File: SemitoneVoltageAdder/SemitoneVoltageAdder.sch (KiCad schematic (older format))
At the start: 9 parts

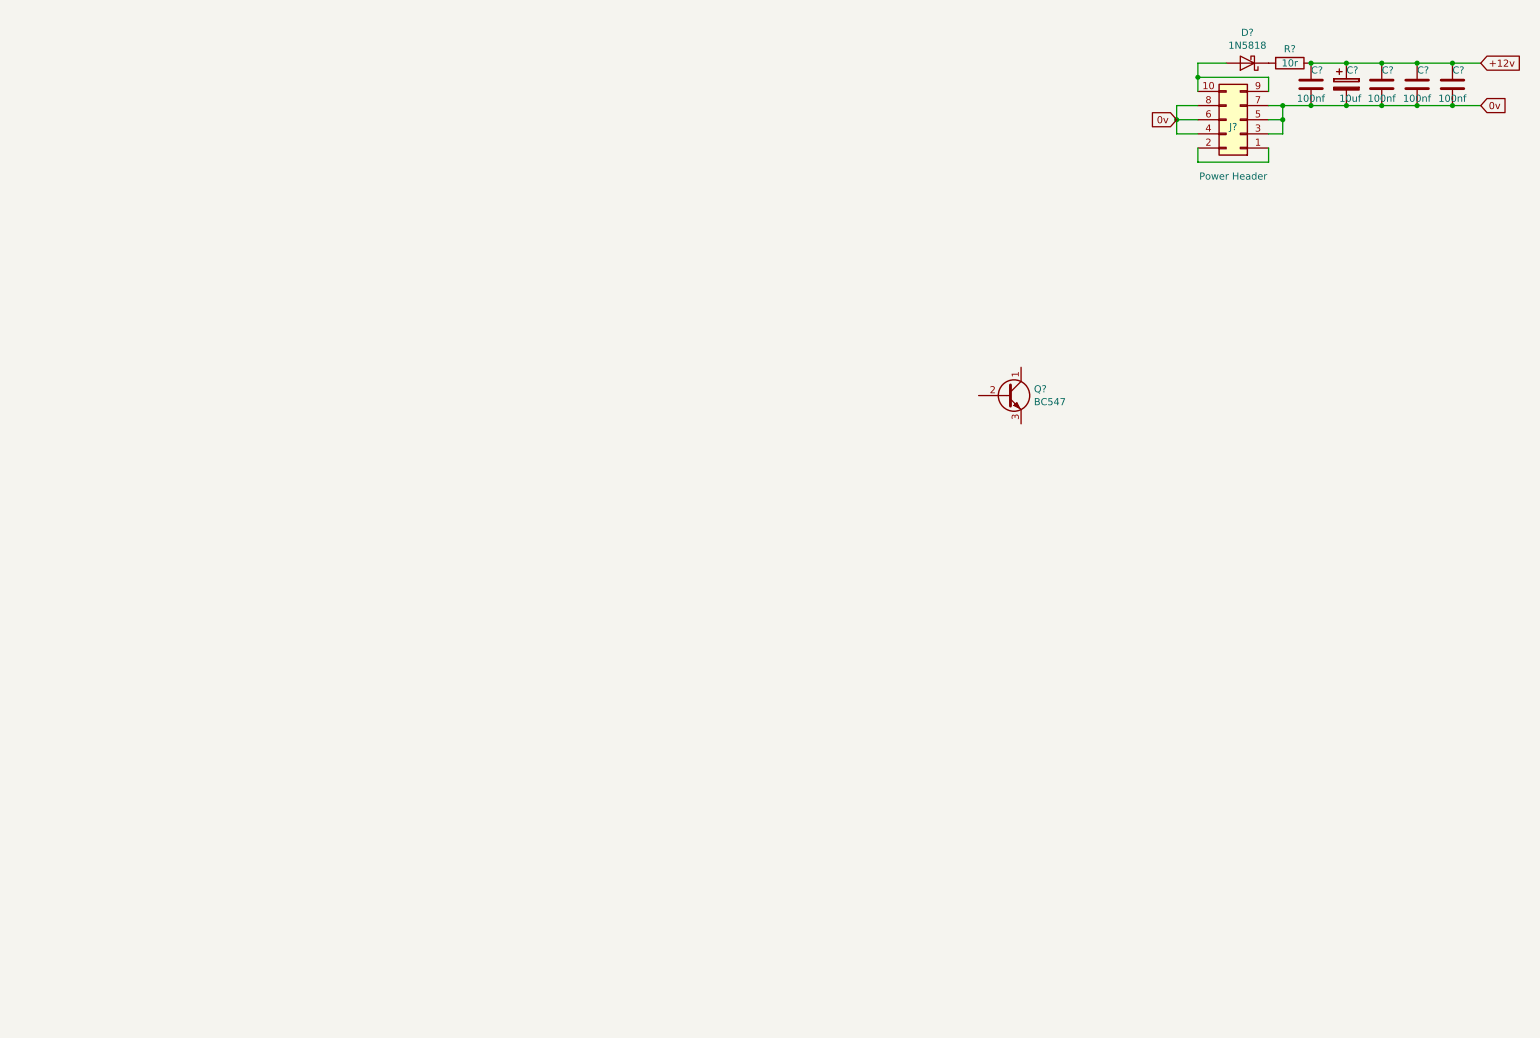
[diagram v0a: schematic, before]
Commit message: Added voltage division, I/O, logic and mixer to the Semitone Voltage Adder
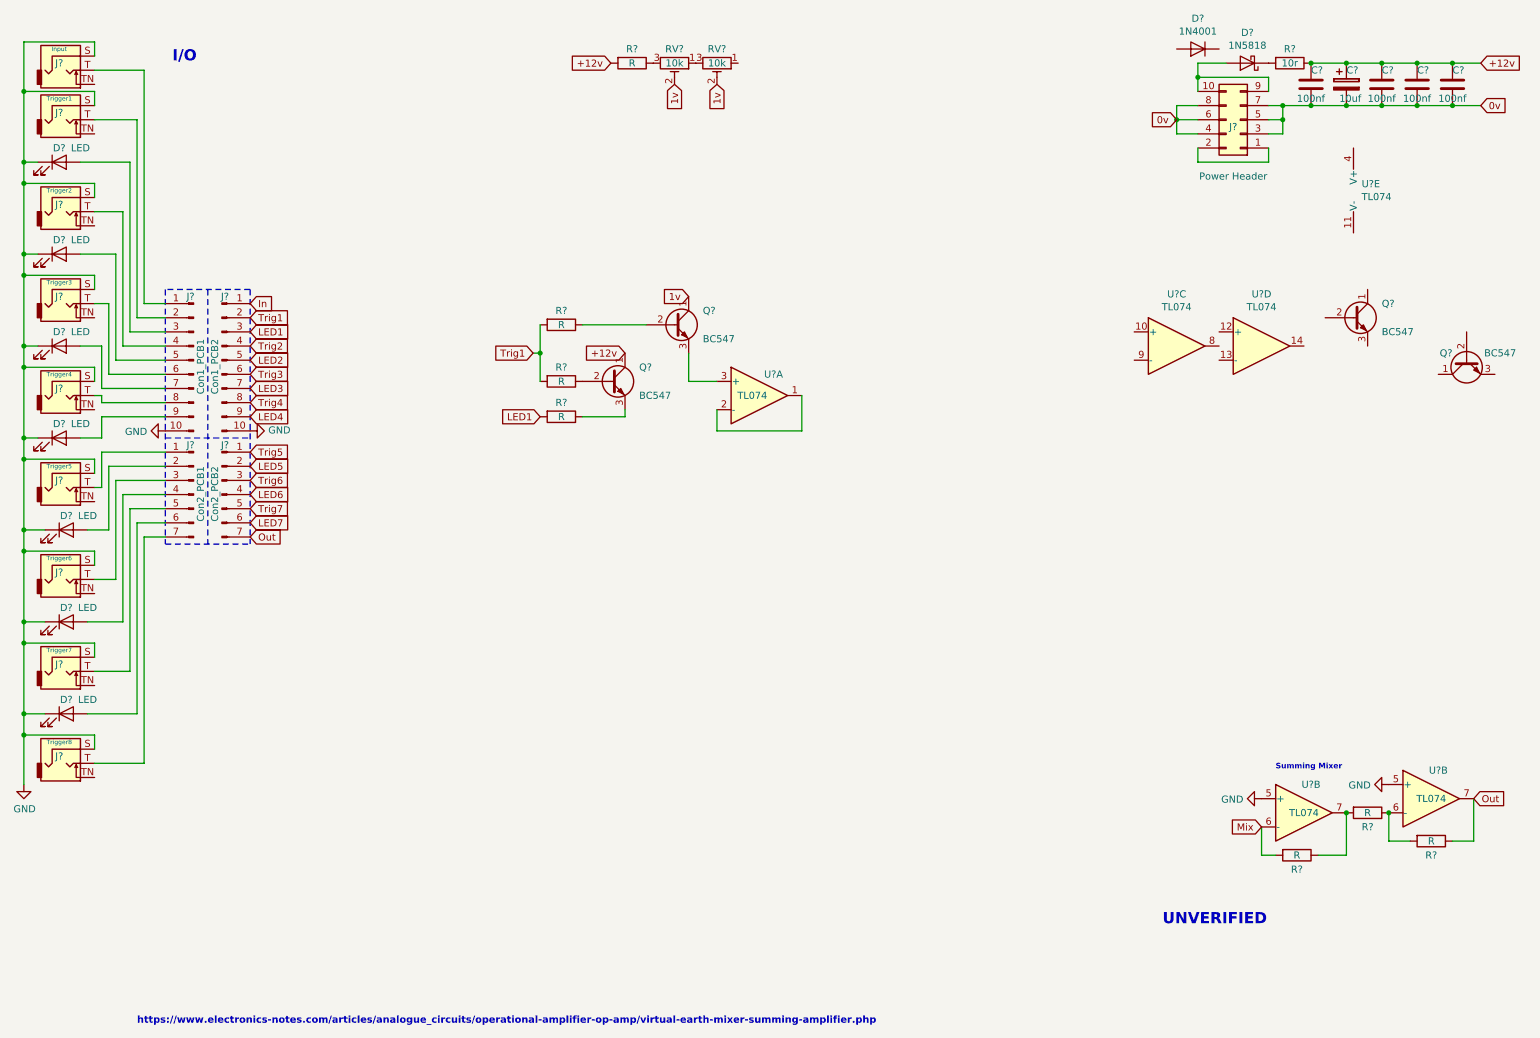
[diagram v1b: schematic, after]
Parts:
- added D? (x7): LED, symbol Device:LED
- added D?: 1N4001, Diode_THT:D_DO-41_SOD81_P10.16mm_Horizontal, symbol Diode:1N4001
- added J?: Input, symbol Connector:AudioJack2_Ground_Switch
- added J?: Trigger1, symbol Connector:AudioJack2_Ground_Switch
- added J?: Trigger2, symbol Connector:AudioJack2_Ground_Switch
- added J?: Trigger3, symbol Connector:AudioJack2_Ground_Switch
- added J?: Trigger4, symbol Connector:AudioJack2_Ground_Switch
- added J?: Trigger5, symbol Connector:AudioJack2_Ground_Switch
- added J?: Trigger6, symbol Connector:AudioJack2_Ground_Switch
- added J?: Trigger7, symbol Connector:AudioJack2_Ground_Switch
- added J?: Trigger8, symbol Connector:AudioJack2_Ground_Switch
- added J?: Con1_PCB1, symbol Connector:Conn_01x10_Male
- added J?: Con2_PCB1, symbol Connector:Conn_01x07_Male
- added J?: Con1_PCB2, symbol Connector:Conn_01x10_Male
- added J?: Con2_PCB2, symbol Connector:Conn_01x07_Male
- added Q? (x3): BC547, Package_TO_SOT_THT:TO-92_Inline, symbol Transistor_BJT:BC547
- added R? (x7): R, symbol Device:R
- added RV? (x2): 10k, symbol Device:R_POT_TRIM
- added U? (x6): TL074, symbol Amplifier_Operational:TL074
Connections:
- net +12v: now also Q?.1 (C), R?.2
- new net: RV?.1, RV?.3
- new net: R?.1, RV?.3
- new net: J?.1 (Pin_1), J?.T (x2)
- new net: Q?.2 (B), R?.1 (x2)
- new net: Q?.3 (E), R?.1
- new net: D?.2 (A), J?.3 (Pin_3)
- new net: Q?.3 (E), U?.3 (+)
- new net: U?.1, U?.2 (-)
- new net: R?.1, R?.2, U?.7
- new net: R?.1, R?.2, U?.6 (-)
- new net: J?.2 (Pin_2), J?.T
- new net: J?.4 (Pin_4), J?.T
- new net: D?.2 (A), J?.5 (Pin_5)
- new net: J?.6 (Pin_6), J?.T
- new net: D?.2 (A), J?.7 (Pin_7)
- new net: J?.8 (Pin_8), J?.T
- new net: D?.2 (A), J?.9 (Pin_9)
- new net: D?.2 (A), J?.2 (Pin_2)
- new net: J?.3 (Pin_3), J?.T
- new net: D?.2 (A), J?.4 (Pin_4)
- new net: J?.5 (Pin_5), J?.T
- new net: D?.2 (A), J?.6 (Pin_6)
- new net: J?.7 (Pin_7), J?.T
- new net 1v: Q?.1 (C), RV?.2, RV?.2
- new net GND: D?.1 (K), D?.1 (K), D?.1 (K), D?.1 (K), D?.1 (K), D?.1 (K), D?.1 (K), J?.10 (Pin_10), J?.10 (Pin_10), J?.S, J?.S, J?.S, J?.S, J?.S, J?.S, J?.S, J?.S, J?.S, U?.5 (+), U?.5 (+)
- new net In: J?.1 (Pin_1)
- new net LED1: J?.3 (Pin_3), R?.2
- new net LED2: J?.5 (Pin_5)
- new net LED3: J?.7 (Pin_7)
- new net LED4: J?.9 (Pin_9)
- new net LED5: J?.2 (Pin_2)
- new net LED6: J?.4 (Pin_4)
- new net LED7: J?.6 (Pin_6)
- new net Mix: R?.2, U?.6 (-)
- new net Out: J?.7 (Pin_7), R?.1, U?.7
- new net Trig1: J?.2 (Pin_2), R?.2, R?.2
- new net Trig2: J?.4 (Pin_4)
- new net Trig3: J?.6 (Pin_6)
- new net Trig4: J?.8 (Pin_8)
- new net Trig5: J?.1 (Pin_1)
- new net Trig6: J?.3 (Pin_3)
- new net Trig7: J?.5 (Pin_5)
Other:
- note added: "I/O"
- note added: "Summing Mixer"
- note added: "UNVERIFIED"
- note added: "https://www.electronics-notes.com/articles/analogue_circuits/operational-amplifier-op-amp/virtual-earth-mixer-summing-amplifier.php"
- moved on the sheet: Q?

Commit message: added buffered mult stage
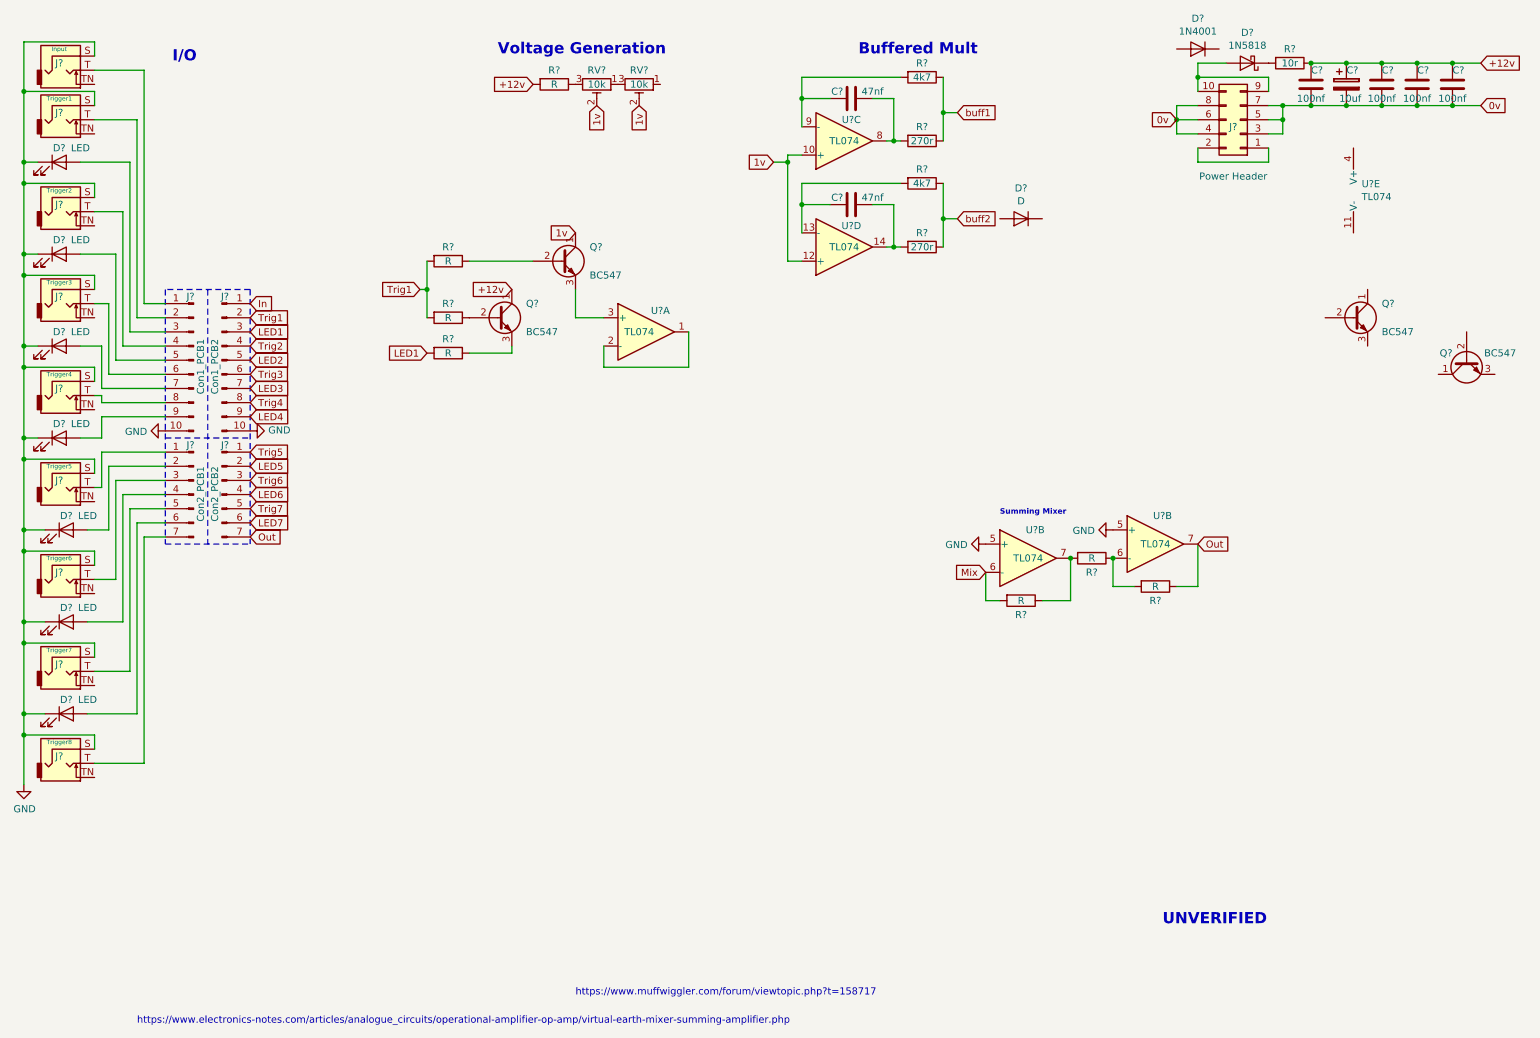
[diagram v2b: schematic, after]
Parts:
- added C? (x2): 47nf, symbol Device:C
- added D?: D, symbol Device:D
- added R? (x2): 270r, symbol Device:R
- added R? (x2): 4k7, symbol Device:R
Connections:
- net 1v: now also U?.10 (+), U?.12 (+)
- net at U?.8: now also C?.1, R?.2
- net at U?.9 (-): now also C?.2, R?.2
- net at U?.13 (-): now also C?.2, R?.2
- net at U?.14: now also C?.1, R?.2
- new net buff1: R?.1, R?.1
- new net buff2: R?.1, R?.1
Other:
- note added: "Buffered Mult"
- note added: "Voltage Generation"
- note added: "https://www.muffwiggler.com/forum/viewtopic.php?t=158717"
- moved on the sheet: Q?, R?, RV?, U?A, U?B, U?C, U?D
